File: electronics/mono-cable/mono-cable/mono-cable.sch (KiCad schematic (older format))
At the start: 4 parts

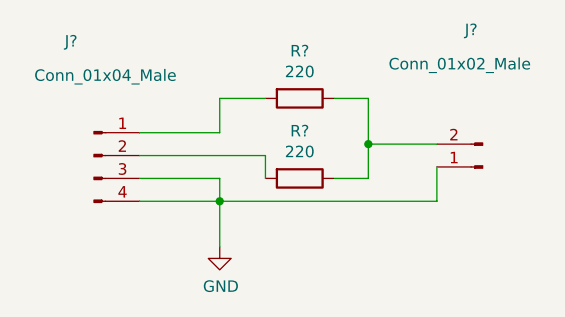
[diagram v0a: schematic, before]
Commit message: Jumpr with empty pin
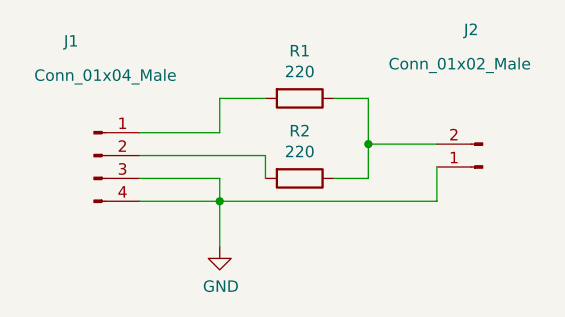
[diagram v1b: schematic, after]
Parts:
- J1: renamed from J?; footprint (none) -> Connector_PinHeader_2.54mm:PinHeader_1x04_P2.54mm_Vertical
- J2: renamed from J?; footprint (none) -> Connector_PinHeader_2.54mm:PinHeader_1x02_P2.54mm_Vertical
- R1, R2: renamed from R?; footprint (none) -> Resistor_THT:R_Axial_DIN0204_L3.6mm_D1.6mm_P7.62mm_Horizontal
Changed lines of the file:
@@
 $EndDescr
 $Comp
-L Connector:Conn_01x04_Male J?
+L Connector:Conn_01x04_Male J1
 U 1 1 5DA9CD94
 P 1600 2700
-F 0 "J?" H 1500 3200 50  0000 C CNN
+F 0 "J1" H 1500 3200 50  0000 C CNN
 F 1 "Conn_01x04_Male" H 1650 3050 50  0000 C CNN
-F 2 "" H 1600 2700 50  0001 C CNN
+F 2 "Connector_PinHeader_2.54mm:PinHeader_1x04_P2.54mm_Vertical" H 1600 2700 50  0001 C CNN
 F 3 "~" H 1600 2700 50  0001 C CNN
 	1    1600 2700
@@
 $EndComp
 $Comp
-L Connector:Conn_01x02_Male J?
+L Connector:Conn_01x02_Male J2
 U 1 1 5DA9D3BB
 P 3300 2750
-F 0 "J?" H 3350 2150 50  0000 C CNN
+F 0 "J2" H 3350 2150 50  0000 C CNN
 F 1 "Conn_01x02_Male" H 3400 2300 50  0000 C CNN
-F 2 "" H 3300 2750 50  0001 C CNN
+F 2 "Connector_PinHeader_2.54mm:PinHeader_1x02_P2.54mm_Vertical" H 3300 2750 50  0001 C CNN
 F 3 "~" H 3300 2750 50  0001 C CNN
 	1    3300 2750
@@
 $EndComp
 $Comp
-L power:GND #PWR?
+L power:GND #PWR01
 U 1 1 5DA9DEEC
 P 2150 3100
-F 0 "#PWR?" H 2150 2850 50  0001 C CNN
+F 0 "#PWR01" H 2150 2850 50  0001 C CNN
 F 1 "GND" H 2155 2927 50  0000 C CNN
 F 2 "" H 2150 3100 50  0001 C CNN
@@
 	3100 2900 3100 2750
 $Comp
-L Device:R R?
+L Device:R R1
 U 1 1 5DA9E7FD
 P 2500 2450
-F 0 "R?" V 2293 2450 50  0000 C CNN
+F 0 "R1" V 2293 2450 50  0000 C CNN
 F 1 "220" V 2384 2450 50  0000 C CNN
-F 2 "" V 2430 2450 50  0001 C CNN
+F 2 "Resistor_THT:R_Axial_DIN0204_L3.6mm_D1.6mm_P7.62mm_Horizontal" V 2430 2450 50  0001 C CNN
 F 3 "~" H 2500 2450 50  0001 C CNN
 	1    2500 2450
@@
 $EndComp
 $Comp
-L Device:R R?
+L Device:R R2
 U 1 1 5DA9F3FD
 P 2500 2800
-F 0 "R?" V 2293 2800 50  0000 C CNN
+F 0 "R2" V 2293 2800 50  0000 C CNN
 F 1 "220" V 2384 2800 50  0000 C CNN
-F 2 "" V 2430 2800 50  0001 C CNN
+F 2 "Resistor_THT:R_Axial_DIN0204_L3.6mm_D1.6mm_P7.62mm_Horizontal" V 2430 2800 50  0001 C CNN
 F 3 "~" H 2500 2800 50  0001 C CNN
 	1    2500 2800
